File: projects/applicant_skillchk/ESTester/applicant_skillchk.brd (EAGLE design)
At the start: 60 x 78 mm, 19 parts, among them J1 3X1A, J2 3X2A, J3 3X2A

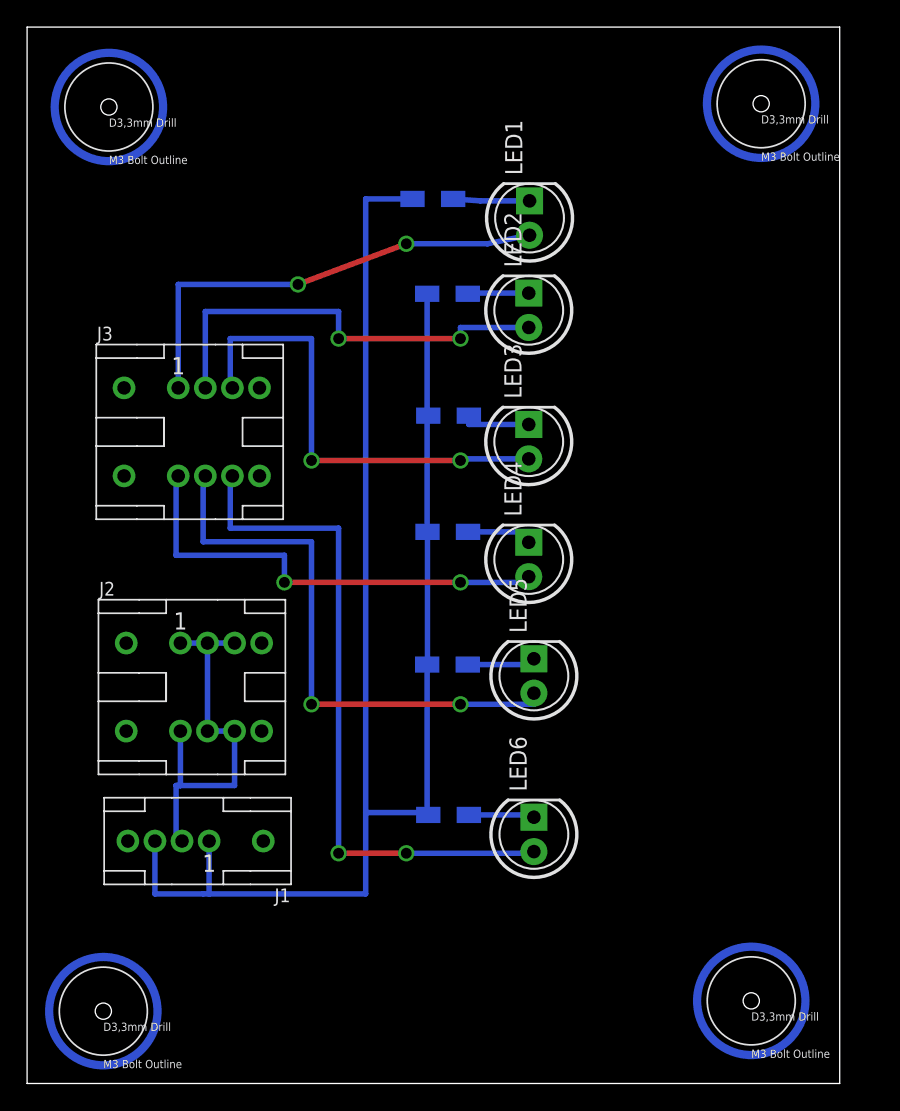
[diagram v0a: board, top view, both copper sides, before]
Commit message: ボード図の修正
ライン間等の圧縮
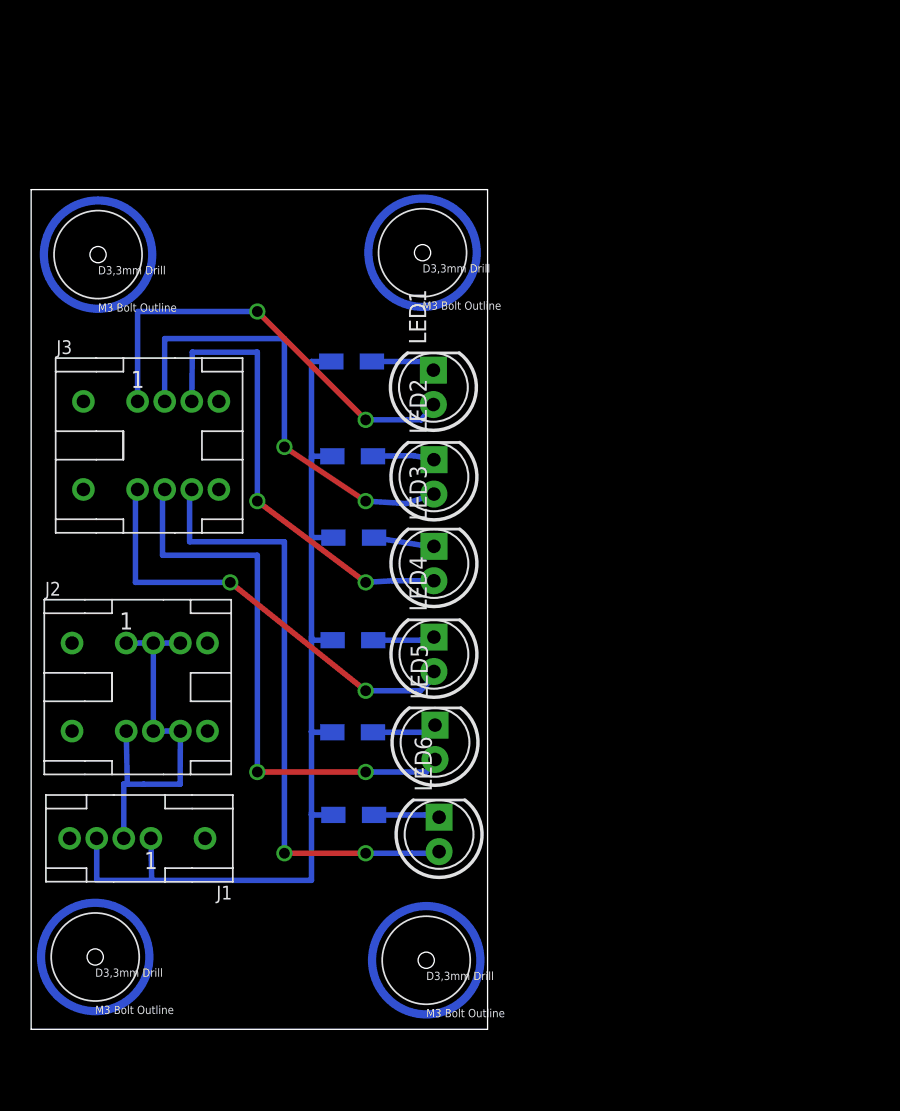
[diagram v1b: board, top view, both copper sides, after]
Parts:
- moved H4 27.3 mm to (29.2, 83.3)
- moved H1 24.2 mm to (29.5, 31.1)
- moved LED1 14.4 mm to (30.0, 73.4)
- moved LED2 14.2 mm to (30.0, 66.8)
- moved R2 13.9 mm to (24.0, 68.3)
- moved R1 13.4 mm to (24.0, 75.3)
- moved LED3 11.4 mm to (30.0, 60.4)
- moved R3 11.4 mm to (24.1, 62.3)
- moved H2 10.9 mm to (5.24, 83.2)
- moved R4 10.6 mm to (24.1, 54.7)
- moved LED4 9.90 mm to (30.0, 53.7)
- moved LED5 8.79 mm to (30.1, 47.2)
- moved R5 8.60 mm to (24.0, 47.9)
- moved LED6 7.00 mm to (30.4, 40.4)
- moved R6 7.00 mm to (24.1, 41.8)
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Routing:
- net GND: track 121.8 -> 71.1 mm
- net N$14: track 50.6 -> 45.6 mm
- net N$9: track 34.2 -> 32.3 mm
- net N$12: track 34.5 -> 32.7 mm
- net N$10: track 32.3 -> 33.9 mm
- net N$6: track 5.25 -> 4.51 mm
- net +5V: track 29.7 -> 29.0 mm
- net N$5: track 5.07 -> 4.47 mm
- net N$13: track 42.3 -> 41.7 mm
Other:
- board size 60 x 78 mm -> 33.7 x 62 mm
